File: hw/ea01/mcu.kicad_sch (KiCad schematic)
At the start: 42 parts, among them J2 USB_B, J3 Conn_01x05_Pin, J8 Conn_01x03_Pin, SW1 SW_Push, SW2 SW_Push, U1 RP2040, U11 W25Q32JVSS, Y1 12Mhz

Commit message: drawing continue..
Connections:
- net BOARD_TEMP: now reaches U1.39 (GPIO27_ADC1)
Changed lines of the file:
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@@
+	(wire
+		(pts
+			(xy 172.72 128.27) (xy 182.88 128.27)
+		)
+		(stroke
+			(width 0)
+			(type default)
+		)
+	)
 	(wire
 		(pts
@@
 			(effects
 				(font
+					(size 1.27 1.27)
+				)
+				(justify left)
+				(hide yes)
+			)
+		)
+	)
+	(global_label "BOARD_TEMP"
+		(shape input)
+		(at 182.88 128.27 0)
+		(fields_autoplaced yes)
+		(effects
+			(font
+				(size 1.27 1.27)
+			)
+			(justify left)
+		)
+		(property "Intersheetrefs" "${INTERSHEET_REFS}"
+			(at 197.8999 128.27 0)
+			(effects
+				(font

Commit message: draw contleted. Not checked yet.
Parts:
- added D1: NUP2105L, Package_TO_SOT_SMD:SOT-23, symbol Power_Protection:NUP2105L
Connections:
- net GND: now also D1.3 (A)
- net UDB_D+: now also D1.1 (K)
- net USB_D-: now also D1.2 (K)
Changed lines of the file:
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@@
 	)
 	(junction
+		(at 62.23 31.75)
+		(diameter 0)
+		(color 0 0 0 0)
+	)
+	(junction
+		(at 67.31 34.29)
+		(diameter 0)
+		(color 0 0 0 0)
+	)
+	(junction
 		(at 220.98 35.56)
 		(diameter 0)
@@
 	(wire
 		(pts
+			(xy 67.31 34.29) (xy 82.55 34.29)
+		)
+		(stroke
+			(width 0)
+			(type default)
+		)
+	)
+	(wire
+		(pts
 			(xy 177.8 24.13) (xy 177.8 22.86)
 		)
@@
 	(wire
 		(pts
-			(xy 36.83 34.29) (xy 82.55 34.29)
+			(xy 36.83 34.29) (xy 67.31 34.29)
 		)
 		(stroke
@@
 	(wire
 		(pts
+			(xy 62.23 31.75) (xy 62.23 39.37)
+		)
+		(stroke
+			(width 0)
+			(type default)
+		)
+	)
+	(wire
+		(pts
 			(xy 207.01 55.88) (xy 207.01 57.15)
 		)
@@
 	(wire
 		(pts
+			(xy 64.77 49.53) (xy 64.77 52.07)
+		)
+		(stroke
+			(width 0)
+			(type default)
+		)
+	)
+	(wire
+		(pts
 			(xy 97.79 140.97) (xy 106.68 140.97)
 		)
@@
 	(wire
 		(pts
-			(xy 36.83 31.75) (xy 85.09 31.75)
+			(xy 36.83 31.75) (xy 62.23 31.75)
 		)
 		(stroke
@@
 	(wire
 		(pts
+			(xy 67.31 34.29) (xy 67.31 39.37)
+		)
+		(stroke
+			(width 0)
+			(type default)
+		)
+	)
+	(wire
+		(pts
 			(xy 163.83 24.13) (xy 163.83 22.86)
 		)
@@
 	(wire
 		(pts
+			(xy 62.23 31.75) (xy 85.09 31.75)
+		)
+		(stroke
+			(width 0)
+			(type default)
+		)
+	)
+	(wire
+		(pts
 			(xy 106.68 74.93) (xy 121.92 74.93)
 		)
@@
 	(symbol
 		(lib_id "power:GND")
+		(at 64.77 52.07 0)
+		(unit 1)
+		(exclude_from_sim no)
+		(in_bom yes)
+		(on_board yes)
+		(dnp no)
+		(fields_autoplaced yes)
+		(property "Reference" "#PWR034"
+			(at 64.77 58.42 0)
+			(effects
+				(font
+					(size 1.27 1.27)
+				)
+				(hide yes)
+			)
+		)
+		(property "Value" "GND"
+			(at 64.77 57.15 0)
+			(effects
+				(font
+					(size 1.27 1.27)
+				)
+			)
+		)
+		(property "Footprint" ""
+			(at 64.77 52.07 0)
+			(effects
+				(font
+					(size 1.27 1.27)
+				)
+				(hide yes)
+			)
+		)
+		(property "Datasheet" ""
+			(at 64.77 52.07 0)
+			(effects
+				(font
+					(size 1.27 1.27)
+				)
+				(hide yes)
+			)
+		)
+		(property "Description" "Power symbol creates a global label with name \"GND\" , ground"
+			(at 64.77 52.07 0)
+			(effects
+				(font
+					(size 1.27 1.27)
+				)
+				(hide yes)
+			)
+		)
+		(pin "1"
+		)
+		(instances
+			(project "ea01"
+				(path "/1c1d47d5-f6ab-48f4-aef9-e333cdfe2713/d3810c5d-87fe-4ffb-a7ba-b811c8939351"
+					(reference "#PWR034")
+					(unit 1)
+				)
+			)
+		)
+	)
+	(symbol
+		(lib_id "power:GND")
 		(at 116.84 184.15 0)
 		(unit 1)
@@
 					(unit 1)
 				)
+			)
+		)
+	)
+	(symbol
+		(lib_id "Power_Protection:NUP2105L")
+		(at 64.77 44.45 0)
+		(unit 1)
+		(exclude_from_sim no)
+		(in_bom yes)
+		(on_board yes)
+		(dnp no)
+		(fields_autoplaced yes)
+		(property "Reference" "D1"
+			(at 71.12 43.1799 0)
+			(effects
+				(font
+					(size 1.27 1.27)
+				)
+				(justify left)
+			)
+		)
+		(property "Value" "NUP2105L"
+			(at 71.12 45.7199 0)
+			(effects
+				(font
+					(size 1.27 1.27)
+				)
+				(justify left)
+			)
+		)
+		(property "Footprint" "Package_TO_SOT_SMD:SOT-23"
+			(at 70.485 45.72 0)
+			(effects
+				(font
+					(size 1.27 1.27)
+				)
+				(justify left)
+				(hide yes)
+			)
+		)
+		(property "Datasheet" "https://www.onsemi.com/pub_link/Collateral/NUP2105L-D.PDF"
+			(at 67.945 41.275 0)
+			(effects
+				(font
+					(size 1.27 1.27)
+				)
+				(hide yes)
+			)
+		)
+		(property "Description" "Dual Line CAN Bus Protector, 24Vrwm"
+			(at 64.77 44.45 0)
+			(effects
+				(font
+					(size 1.27 1.27)
+				)
+				(hide yes)
+			)
+		)
+		(pin "1"
+		)
+		(pin "2"
+		)
+		(pin "3"
+		)
+		(instances
+			(project ""
+				(path "/1c1d47d5-f6ab-48f4-aef9-e333cdfe2713/d3810c5d-87fe-4ffb-a7ba-b811c8939351"
+					(reference "D1")
+					(unit 1)
+				)

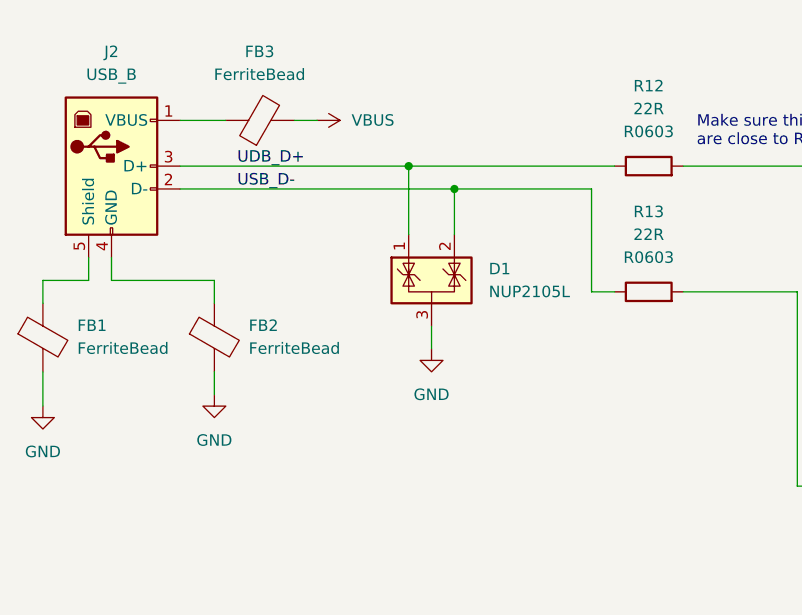
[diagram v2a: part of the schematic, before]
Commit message: 3d models updated
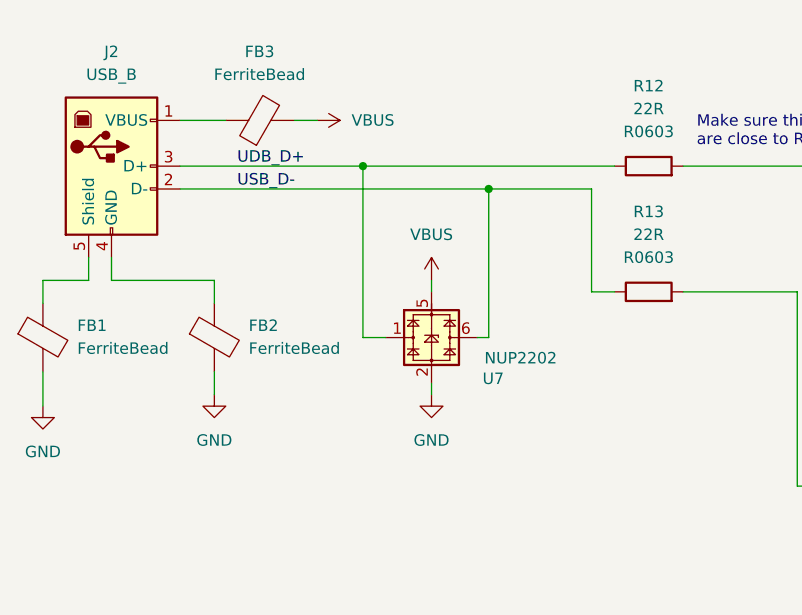
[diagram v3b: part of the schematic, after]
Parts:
- removed D1: NUP2105L, Package_TO_SOT_SMD:SOT-23, symbol Power_Protection:NUP2105L
- added U7: NUP2202, Package_TO_SOT_SMD:SOT-363_SC-70-6, symbol Power_Protection:NUP2202
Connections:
- net GND: now also U7.2
- net UDB_D+: now also U7.1
- net USB_D-: now also U7.6
- net VBUS: now also U7.5
